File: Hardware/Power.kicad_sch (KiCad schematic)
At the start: 23 parts, among them U1 AMS1117-5.0, U2 AMS1117-3.3, X1 PEDAL_COMBO_TOP

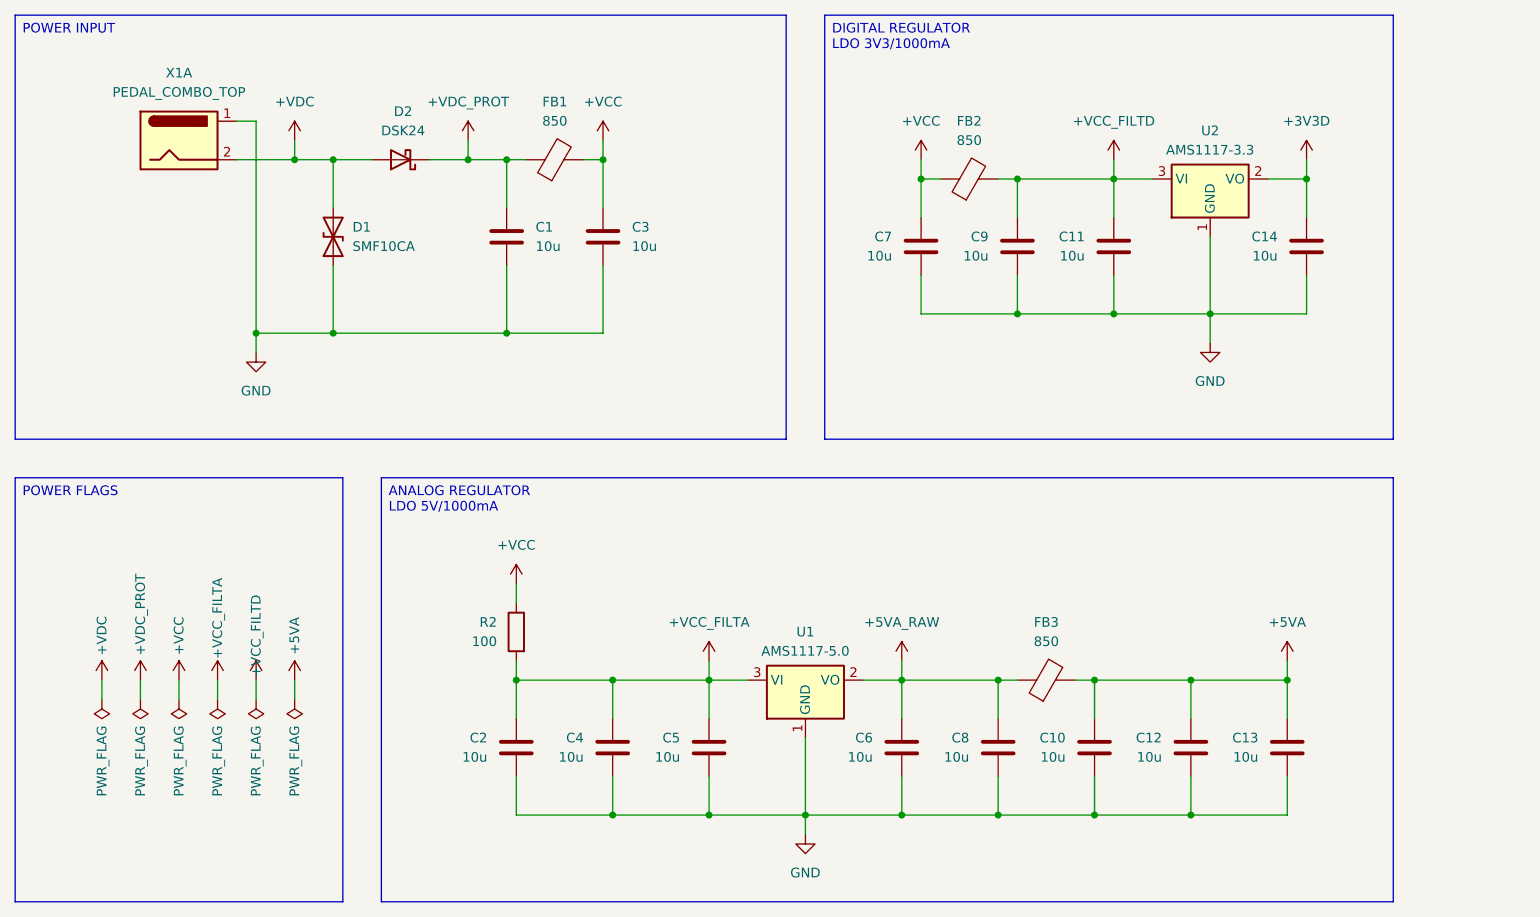
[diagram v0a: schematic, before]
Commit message: Layout review
Updated the LDO layout to include a series resistor for stability.
Updated all build files.
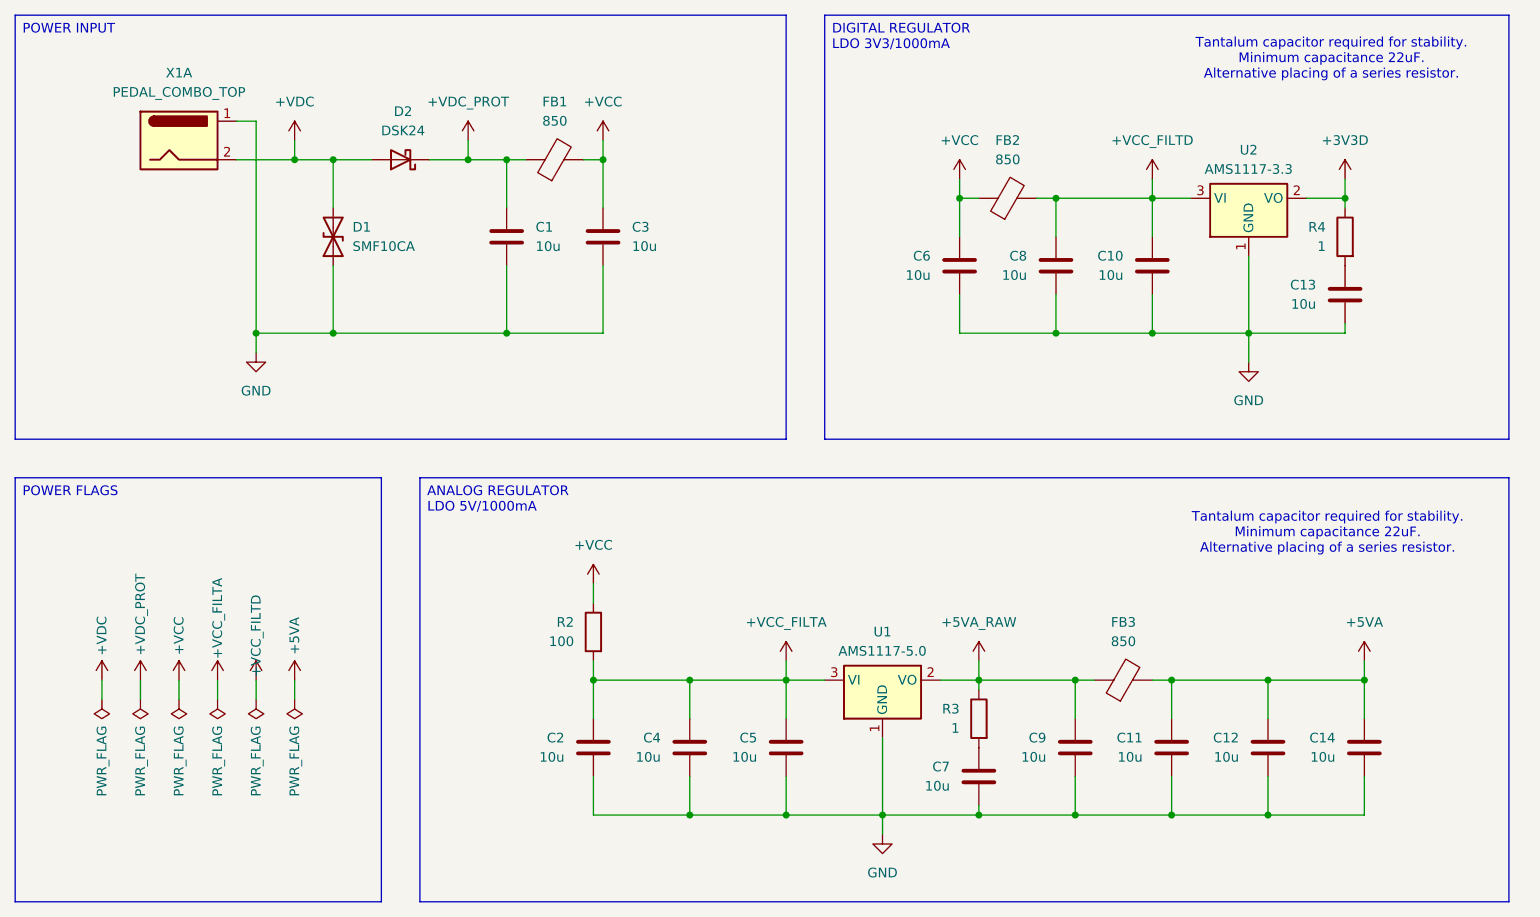
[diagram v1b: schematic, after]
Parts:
- removed C14, C6: 10u, Capacitor_SMD:C_0805_2012Metric, symbol Device:C
- added C13, C7: 10u, Capacitor_SMD:C_0805_2012Metric, symbol Device:C
- added R3, R4: 1, Resistor_SMD:R_0603_1608Metric, symbol Device:R
- renumbered C11 to C10, C10 to C11, C13 to C14, C7 to C6, C9 to C8, C8 to C9
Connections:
- net +3V3D: now also R4.1
- net +5VA_RAW: now also R3.1
- net GND: now also C13.2, C7.2
- new net: C7.1, R3.2
- new net: C13.1, R4.2
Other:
- note added: "Tantalum capacitor required for stability. Minimum capacitance 22uF. Alternative placing of a series resistor."
- moved on the sheet: C10, C11, C12, C14, C2, C4, C5, C6, C8, C9, FB2, FB3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

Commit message: Output files
Updated the board silkscreen.
Upddated the output files.
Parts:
- C1, C10, C11, C12, C13, C14, C2, C3, C4, C5, C6, C7, C8, C9: JLCPCB Part (none) -> C15850; Manufacturer Part (none) -> CL21A106KAYNNNE
- D1: JLCPCB Part (none) -> C19077505; Manufacturer Part (none) -> SMF10CA
- D2: JLCPCB Part (none) -> C22466352; Manufacturer Part (none) -> DSK24
- FB1, FB2, FB3: JLCPCB Part (none) -> C13415; Manufacturer Part (none) -> SDCL1608C68NJTDF
- R2: JLCPCB Part (none) -> C22775; Manufacturer Part (none) -> 0603WAF1000T5E
- R3, R4: JLCPCB Part (none) -> C22936; Manufacturer Part (none) -> 0603WAF100KT5E
- U1: JLCPCB Part (none) -> C6187; Manufacturer Part (none) -> AMS1117-5.0
- U2: JLCPCB Part (none) -> C6186; Manufacturer Part (none) -> AMS1117-3.3
- X1: now left out of the parts list
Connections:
- net +3V3D: now also C13.1; no longer R4.1
- net +5VA_RAW: now also C7.1; no longer R3.1
- net GND: now also R3.2, R4.2; no longer C13.2, C7.2
- new net: C7.2, R3.1
- new net: C13.2, R4.1
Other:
- moved on the sheet: C13, C7, R3, R4

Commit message: Assembly review
Performed a full review of the schematic and layout.
Minor changes to the schematic and layout.
Updated output files.
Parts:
- X1: JLCPCB Part (none) -> -; Manufacturer Part (none) -> -
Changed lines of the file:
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@@
+			)
+		)
+		(property "JLCPCB Part" "-"
+			(at 80.01 46.99 0)
+			(hide yes)
+			(show_name no)
+			(do_not_autoplace no)
+			(effects
+				(font
+					(size 1.27 1.27)
+				)
+			)
+		)
+		(property "Manufacturer Part" "-"
+			(at 80.01 46.99 0)
+			(hide yes)
+			(show_name no)
+			(do_not_autoplace no)
+			(effects
+				(font
+					(size 1.27 1.27)
+				)
 			)
 		)

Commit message: Initial software release
Added an initial sine generator application.
Only the I2S output is working via PIO.
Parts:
- R2: value 100 -> 10; JLCPCB Part C22775 -> C22859; Manufacturer Part 0603WAF1000T5E -> 0603WAF100JT5E
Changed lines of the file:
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@@
 			)
 		)
-		(property "Value" "100"
+		(property "Value" "10"
 			(at 132.08 113.0299 0)
 			(show_name no)
@@
 			)
 		)
-		(property "JLCPCB Part" "C22775"
+		(property "JLCPCB Part" "C22859"
 			(at 134.62 111.76 0)
 			(hide yes)
@@
 			)
 		)
-		(property "Manufacturer Part" "0603WAF1000T5E"
+		(property "Manufacturer Part" "0603WAF100JT5E"
 			(at 134.62 111.76 0)
 			(hide yes)
